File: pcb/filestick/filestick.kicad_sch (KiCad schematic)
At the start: 108 parts, among them J1 DIN-5_180degree, J2 Micro_SD_Card_Det2, J3 USB_B_Micro, J4 DIN-5_180degree, J5 Conn_01x09_Pin, J6 Conn_01x02_Pin, J7 Conn_01x02_Pin, J8 Conn_02x08_Odd_Even, J9 Conn_01x08_Pin, Q1 2N7002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

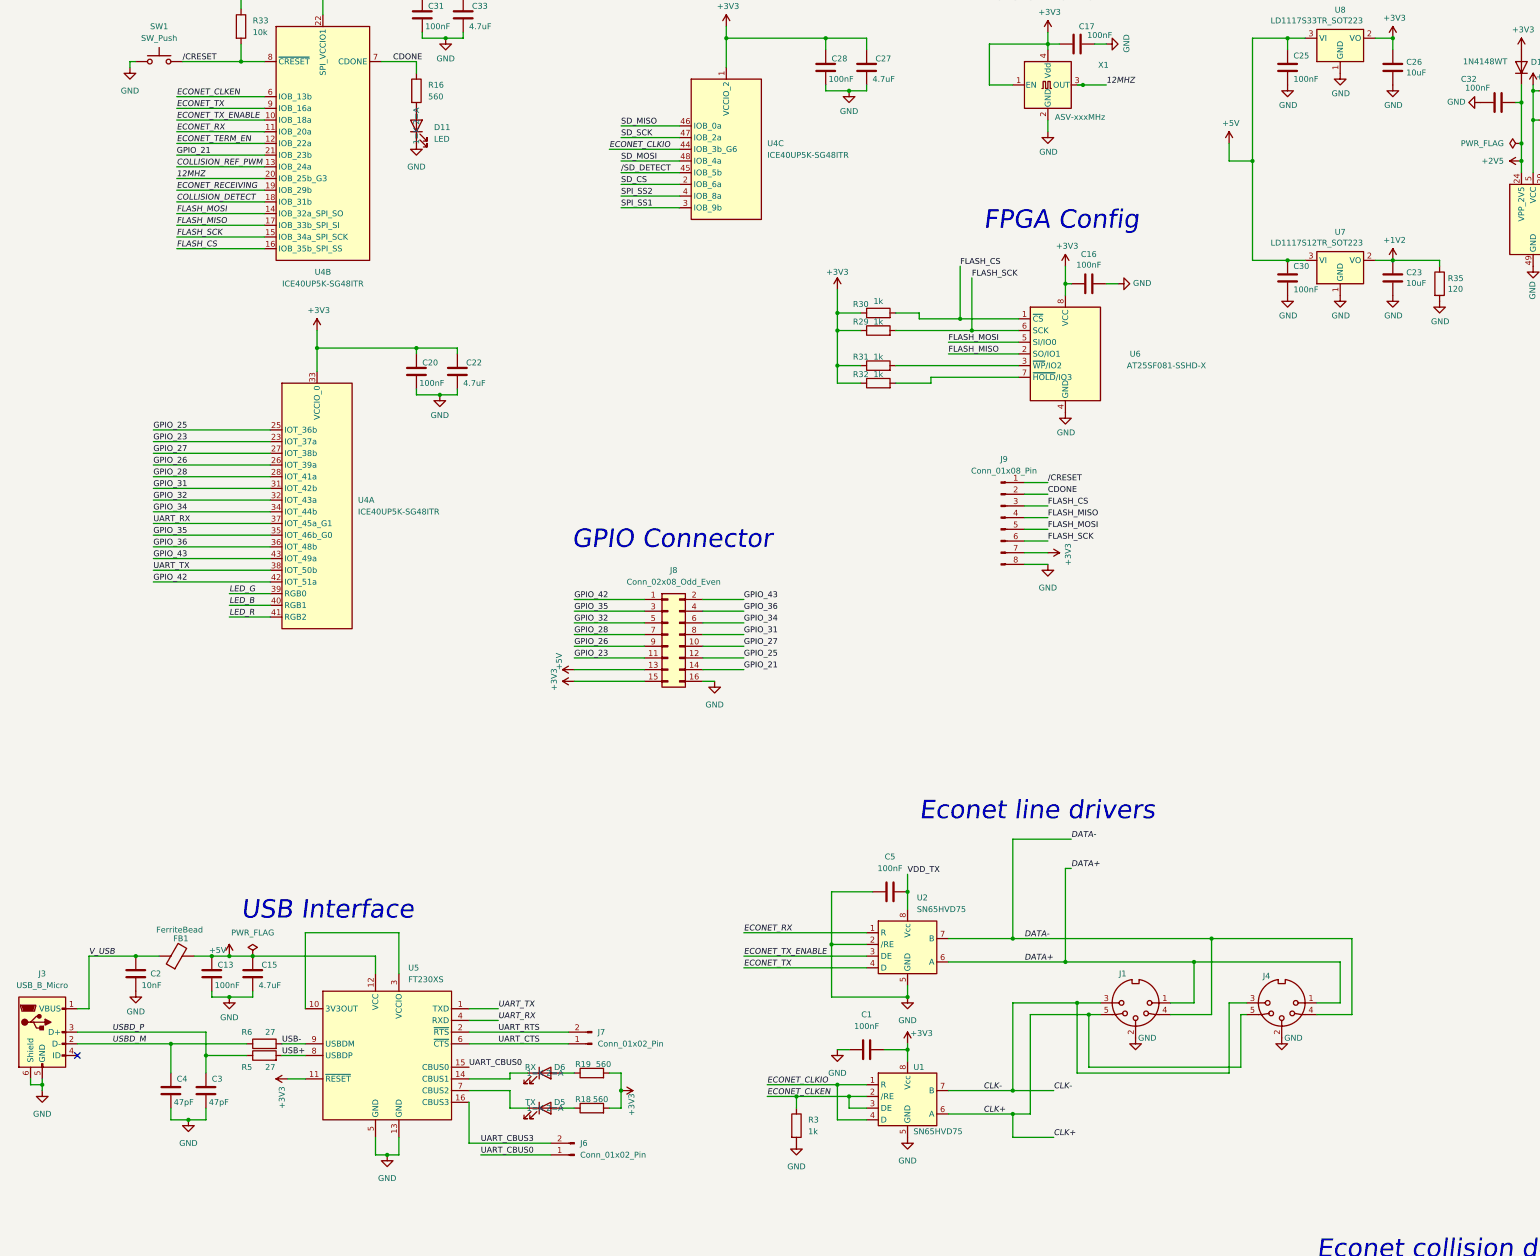
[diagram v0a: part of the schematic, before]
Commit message: Add USB power soft start, CTS and RTS
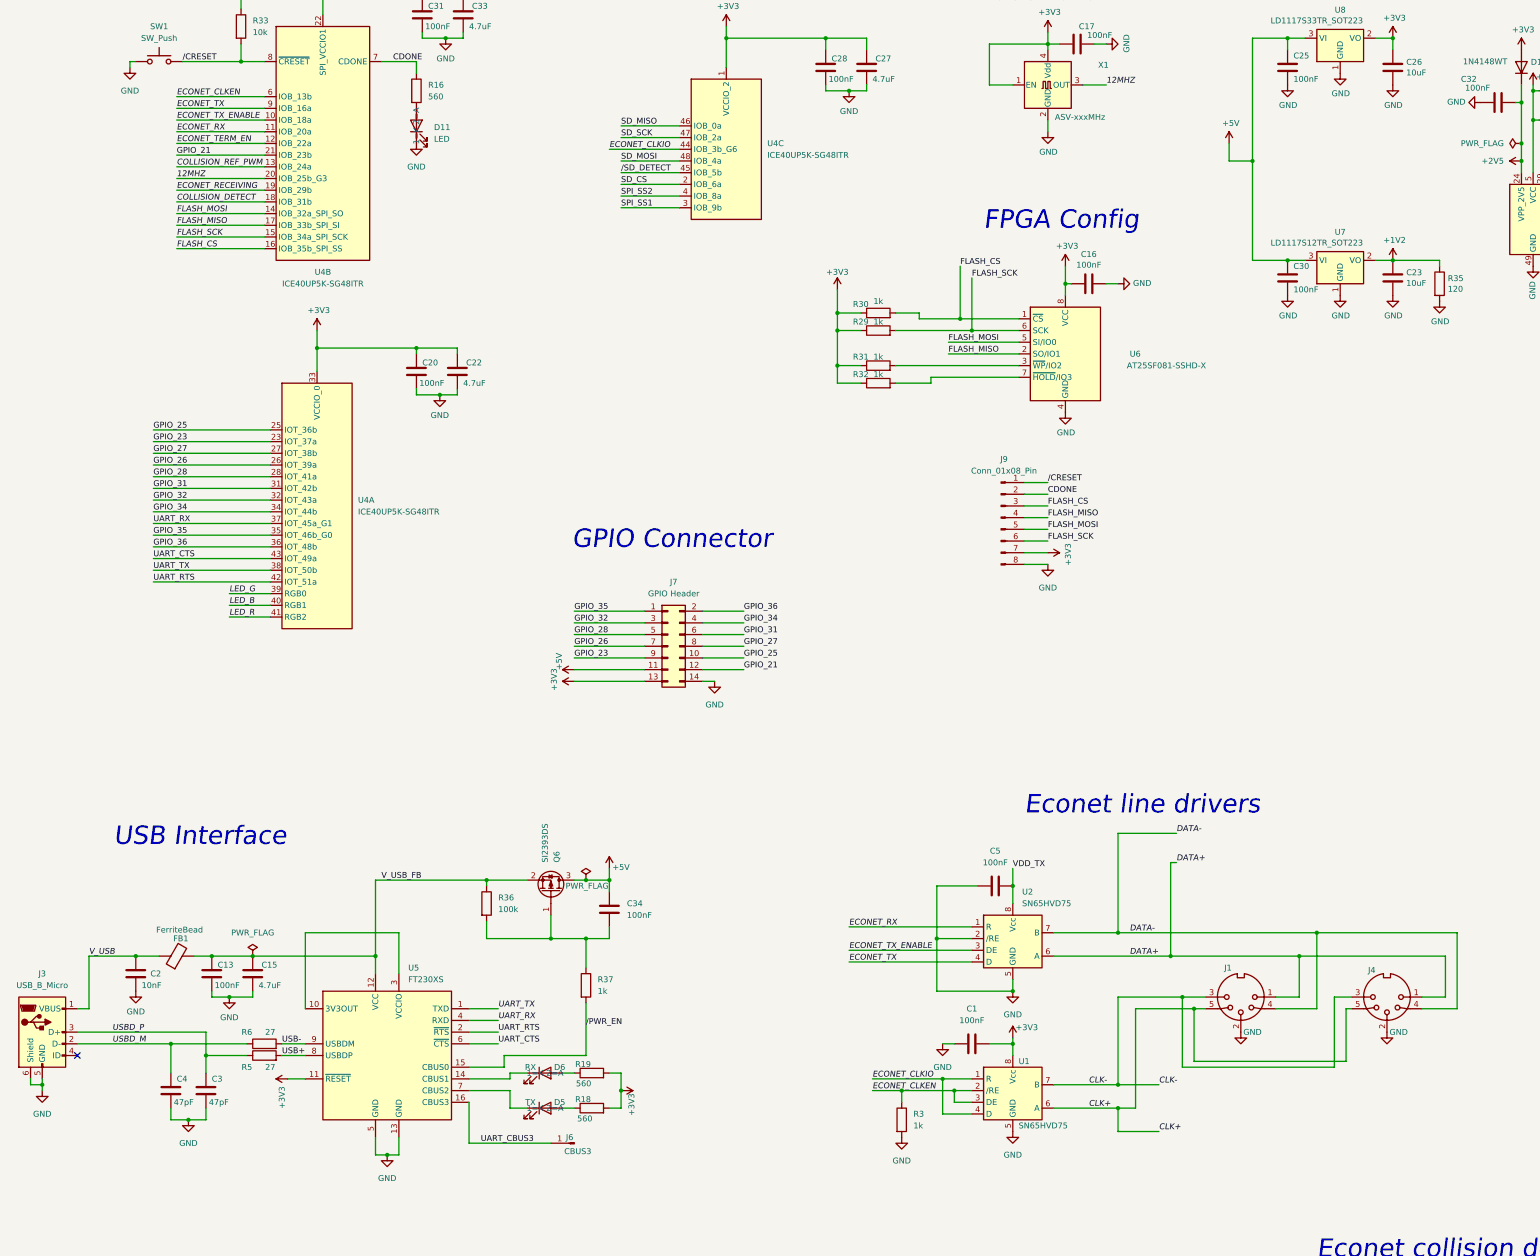
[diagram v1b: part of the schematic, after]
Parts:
- removed J6, J7: Conn_01x02_Pin, Connector_PinHeader_2.54mm:PinHeader_1x02_P2.54mm_Vertical, symbol Connector:Conn_01x02_Pin
- removed J8: Conn_02x08_Odd_Even, Connector_PinHeader_2.54mm:PinHeader_2x08_P2.54mm_Vertical, symbol Connector_Generic:Conn_02x08_Odd_Even
- added C34: 100nF, symbol Device:C
- added J6: CBUS3, symbol Connector:Conn_01x01_Pin
- added J7: GPIO Header, symbol Connector_Generic:Conn_02x07_Odd_Even
- added Q6: SI2393DS, Package_TO_SOT_SMD:SOT-23, symbol Transistor_FET:Q_PMOS_GSD
- added R36: 100k, symbol Device:R
- added R37: 1k, symbol Device:R
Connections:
- net GPIO_42 is gone; now on net UART_RTS: U4.42 (IOT_51a)
- net GPIO_43 is gone; now on net UART_CTS: U4.43 (IOT_49a)
- net +3V3: now also J7.13 (Pin_13)
- net +5V: now also C34.1, J7.11 (Pin_11), Q6.3 (D); no longer C13.2, C15.2, FB1.2, U5.12 (VCC)
- net GND: now also J7.14 (Pin_14)
- net GPIO_21: now also J7.12 (Pin_12)
- net GPIO_23: now also J7.9 (Pin_9)
- net GPIO_25: now also J7.10 (Pin_10)
- net GPIO_26: now also J7.7 (Pin_7)
- net GPIO_27: now also J7.8 (Pin_8)
- net GPIO_28: now also J7.5 (Pin_5)
- net GPIO_31: now also J7.6 (Pin_6)
- net GPIO_32: now also J7.3 (Pin_3)
- net GPIO_34: now also J7.4 (Pin_4)
- net GPIO_35: now also J7.1 (Pin_1)
- net GPIO_36: now also J7.2 (Pin_2)
- net UART_CBUS3: now also J6.1 (Pin_1)
- net UART_CBUS0 renamed /PWR_EN
- net /PWR_EN: now also R37.2
- new net: C34.2, Q6.1 (G), R36.2, R37.1
- new net V_USB_FB: C13.2, C15.2, FB1.2, Q6.2 (S), R36.1, U5.12 (VCC)
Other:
- moved on the sheet: C1, C5, J1, J4, R3, U1, U2
